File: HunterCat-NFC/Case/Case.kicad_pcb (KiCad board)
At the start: 2 copper layers, 80.7 x 33.5 mm, 10 parts

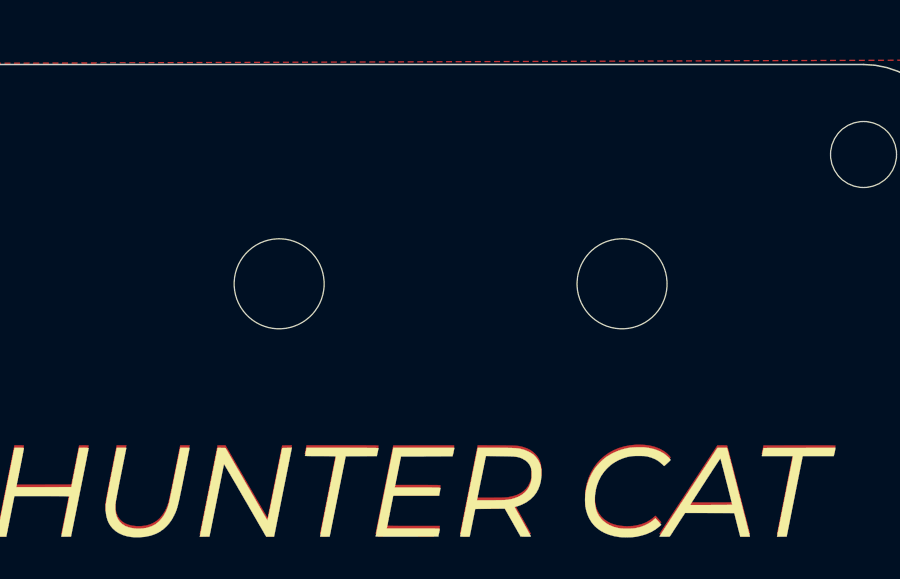
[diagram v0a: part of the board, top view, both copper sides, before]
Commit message: Symmetric design (case and acrylic)
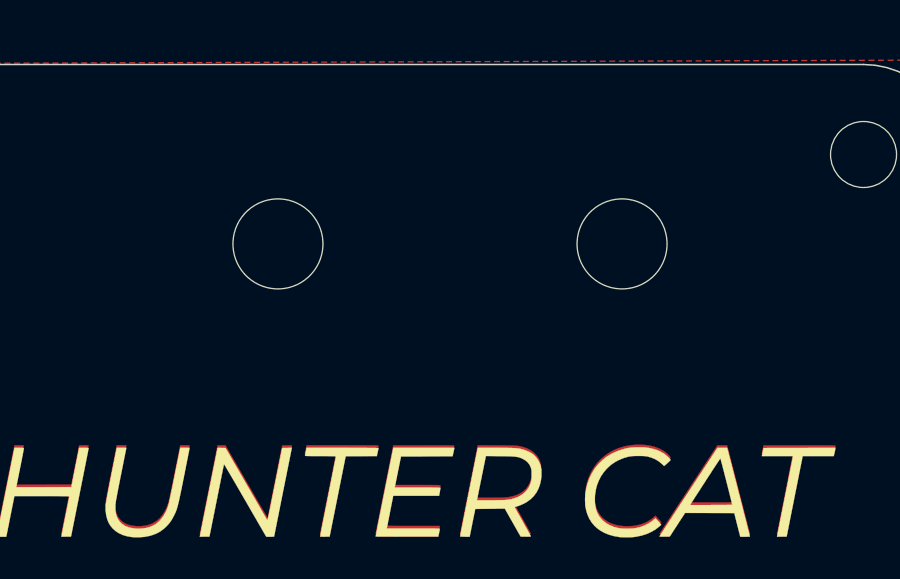
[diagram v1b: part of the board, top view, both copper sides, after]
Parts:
- removed the REF** at (138.3, 82.8)
- removed the REF** at (149.6, 82.8)
- added REF**: MountingHole_2.2mm_M2, MountingHole:MountingHole_2.2mm_M2, F.Cu at (138.2, 81.5)
- added REF**: MountingHole_2.2mm_M2, MountingHole:MountingHole_2.2mm_M2, F.Cu at (149.6, 81.5)
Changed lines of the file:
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@@
-(kicad_pcb (version 20171130) (host pcbnew "(5.1.6-0-10_14)")
+(kicad_pcb (version 20171130) (host pcbnew "(5.1.5)-3")
   (general
     (thickness 1.6)
-    (drawings 30)
+    (drawings 29)
     (tracks 0)
     (zones 0)
@@
   )
   (module MountingHole:MountingHole_2.2mm_M2 (layer F.Cu)
-    (at 138.3 82.81)
+    (at 138.17 81.48)
     (descr "Mounting Hole 2.2mm, no annular, M2")
     (tags "mounting hole 2.2mm no annular m2")
@@
       (effects (font (size 1 1) (thickness 0.15)))
     )
-    (pad "" np_thru_hole circle (at -0.09 0) (size 3 3) (drill 3) (layers *.Cu *.Mask))
+    (pad "" np_thru_hole circle (at 0 0) (size 3 3) (drill 3) (layers *.Cu *.Mask))
+  )
+  (module MountingHole:MountingHole_2.2mm_M2 (layer F.Cu)
+    (at 138.21 103.02)
+    (descr "Mounting Hole 2.2mm, no annular, M2")
+    (tags "mounting hole 2.2mm no annular m2")
+    (attr virtual)
+    (fp_text reference REF** (at 0 -3.2) (layer F.Fab)
+      (effects (font (size 1 1) (thickness 0.15)))
+    )
+    (fp_text value MountingHole_2.2mm_M2 (at 0 3.2) (layer F.Fab)
+      (effects (font (size 1 1) (thickness 0.15)))
+    )
+    (fp_text user %R (at 0.3 0) (layer F.Fab)
+      (effects (font (size 1 1) (thickness 0.15)))
+    )
+    (fp_circle (center 0 0) (end 2.45 0) (layer F.CrtYd) (width 0.05))
+    (fp_circle (center 0 0) (end 2.2 0) (layer Cmts.User) (width 0.15))
+    (pad "" np_thru_hole circle (at 0 0) (size 3 3) (drill 3) (layers *.Cu *.Mask))
+  )
+  (module MountingHole:MountingHole_2.2mm_M2 (layer F.Cu)
+    (at 149.64 103.02)
+    (descr "Mounting Hole 2.2mm, no annular, M2")
+    (tags "mounting hole 2.2mm no annular m2")
+    (attr virtual)
+    (fp_text reference REF** (at 0 -3.2) (layer F.Fab)
+      (effects (font (size 1 1) (thickness 0.15)))
+    )
+    (fp_text value MountingHole_2.2mm_M2 (at 0 3.2) (layer F.Fab)
+      (effects (font (size 1 1) (thickness 0.15)))
+    )
+    (fp_circle (center 0 0) (end 2.2 0) (layer Cmts.User) (width 0.15))
+    (fp_circle (center 0 0) (end 2.45 0) (layer F.CrtYd) (width 0.05))
+    (fp_text user %R (at 0.3 0) (layer F.Fab)
+      (effects (font (size 1 1) (thickness 0.15)))
+    )
+    (pad "" np_thru_hole circle (at 0 0) (size 3 3) (drill 3) (layers *.Cu *.Mask))
+  )
+  (module MountingHole:MountingHole_2.2mm_M2 (layer F.Cu)
+    (at 149.64 81.48)
+    (descr "Mounting Hole 2.2mm, no annular, M2")
+    (tags "mounting hole 2.2mm no annular m2")
+    (attr virtual)
+    (fp_text reference REF** (at 0 -3.2) (layer F.Fab)
+      (effects (font (size 1 1) (thickness 0.15)))
+    )
+    (fp_text value MountingHole_2.2mm_M2 (at 0 3.2) (layer F.Fab)
+      (effects (font (size 1 1) (thickness 0.15)))
+    )
+    (fp_text user %R (at 0.3 0) (layer F.Fab)
+      (effects (font (size 1 1) (thickness 0.15)))
+    )
+    (fp_circle (center 0 0) (end 2.45 0) (layer F.CrtYd) (width 0.05))
+    (fp_circle (center 0 0) (end 2.2 0) (layer Cmts.User) (width 0.15))
+    (pad "" np_thru_hole circle (at 0 0) (size 3 3) (drill 3) (layers *.Cu *.Mask))
   )
   (module "Ilustracion Final HC-NFC" (layer B.Cu)
@@
   )
   (module MountingHole:MountingHole_2.2mm_M2 (layer F.Cu)
-    (at 138.21 103.02)
-    (descr "Mounting Hole 2.2mm, no annular, M2")
-    (tags "mounting hole 2.2mm no annular m2")
-    (attr virtual)
-    (fp_text reference REF** (at 0 -3.2) (layer F.Fab)
-      (effects (font (size 1 1) (thickness 0.15)))
-    )
-    (fp_text value MountingHole_2.2mm_M2 (at 0 3.2) (layer F.Fab)
-      (effects (font (size 1 1) (thickness 0.15)))
-    )
-    (fp_circle (center 0 0) (end 2.2 0) (layer Cmts.User) (width 0.15))
-    (fp_circle (center 0 0) (end 2.45 0) (layer F.CrtYd) (width 0.05))
-    (fp_text user %R (at 0.3 0) (layer F.Fab)
-      (effects (font (size 1 1) (thickness 0.15)))
-    )
-    (pad "" np_thru_hole circle (at 0 0) (size 3 3) (drill 3) (layers *.Cu *.Mask))
-  )
-  (module MountingHole:MountingHole_2.2mm_M2 (layer F.Cu)
     (at 157.69 78.5)
     (descr "Mounting Hole 2.2mm, no annular, M2")
@@
   )
   (module MountingHole:MountingHole_2.2mm_M2 (layer F.Cu)
-    (at 149.64 103.02)
-    (descr "Mounting Hole 2.2mm, no annular, M2")
-    (tags "mounting hole 2.2mm no annular m2")
-    (attr virtual)
-    (fp_text reference REF** (at 0 -3.2) (layer F.Fab)
-      (effects (font (size 1 1) (thickness 0.15)))
-    )
-    (fp_text value MountingHole_2.2mm_M2 (at 0 3.2) (layer F.Fab)
-      (effects (font (size 1 1) (thickness 0.15)))
-    )
-    (fp_circle (center 0 0) (end 2.2 0) (layer Cmts.User) (width 0.15))
-    (fp_circle (center 0 0) (end 2.45 0) (layer F.CrtYd) (width 0.05))
-    (fp_text user %R (at 0.3 0) (layer F.Fab)
-      (effects (font (size 1 1) (thickness 0.15)))
-    )
-    (pad "" np_thru_hole circle (at 0 0) (size 3 3) (drill 3) (layers *.Cu *.Mask))
-  )
-  (module MountingHole:MountingHole_2.2mm_M2 (layer F.Cu)
-    (at 149.64 82.81)
-    (descr "Mounting Hole 2.2mm, no annular, M2")
-    (tags "mounting hole 2.2mm no annular m2")
-    (attr virtual)
-    (fp_text reference REF** (at 0 -3.2) (layer F.Fab)
-      (effects (font (size 1 1) (thickness 0.15)))
-    )
-    (fp_text value MountingHole_2.2mm_M2 (at 0 3.2) (layer F.Fab)
-      (effects (font (size 1 1) (thickness 0.15)))
-    )
-    (fp_circle (center 0 0) (end 2.45 0) (layer F.CrtYd) (width 0.05))
-    (fp_circle (center 0 0) (end 2.2 0) (layer Cmts.User) (width 0.15))
-    (fp_text user %R (at 0.3 0) (layer F.Fab)
-      (effects (font (size 1 1) (thickness 0.15)))
-    )
-    (pad "" np_thru_hole circle (at 0 0) (size 3 3) (drill 3) (layers *.Cu *.Mask))
-  )
-  (module MountingHole:MountingHole_2.2mm_M2 (layer F.Cu)
     (at 157.69 105.99)
     (descr "Mounting Hole 2.2mm, no annular, M2")
@@
     (arrow2b (pts (xy 105.46 104.49) (xy 104.873579 103.363496)))
   )
-  (dimension 4.5 (width 0.05) (layer F.CrtYd)
-    (gr_text "4.500 mm" (at 105.11 77.75 270) (layer F.CrtYd)
-      (effects (font (size 1 1) (thickness 0.15)))
-    )
-    (feature1 (pts (xy 107.4 80) (xy 105.723579 80)))
-    (feature2 (pts (xy 107.4 75.5) (xy 105.723579 75.5)))
-    (crossbar (pts (xy 106.31 75.5) (xy 106.31 80)))
-    (arrow1a (pts (xy 106.31 80) (xy 105.723579 78.873496)))
-    (arrow1b (pts (xy 106.31 80) (xy 106.896421 78.873496)))
-    (arrow2a (pts (xy 106.31 75.5) (xy 105.723579 76.626504)))
-    (arrow2b (pts (xy 106.31 75.5) (xy 106.896421 76.626504)))
-  )
   (dimension 4.51 (width 0.05) (layer F.CrtYd)
